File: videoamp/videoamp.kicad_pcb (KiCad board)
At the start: 2 copper layers, 19 x 26 mm, 20 parts, among them J5V1 Conn_01x01, U1 THS7316, U2 AMS1117-3.3

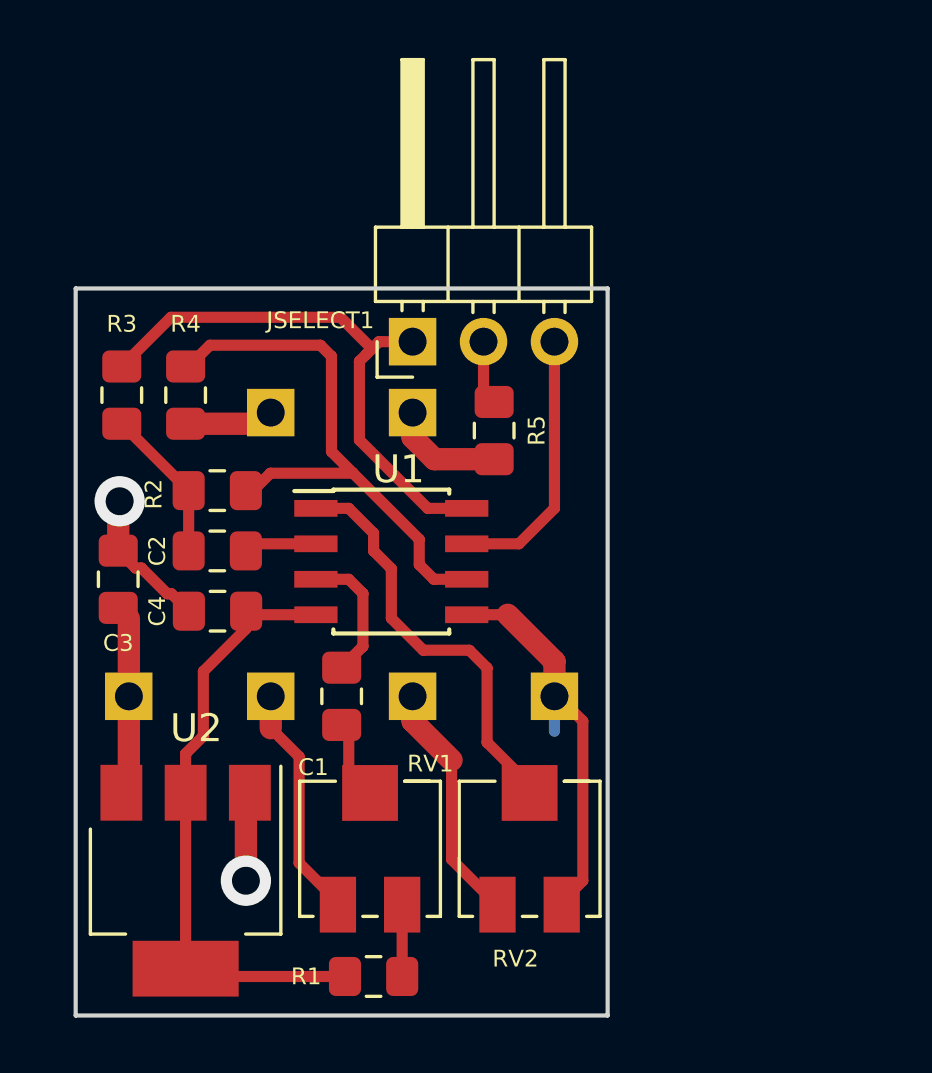
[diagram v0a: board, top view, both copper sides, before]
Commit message: Redesign board to provide luma/chroma/composite signals on A/V out
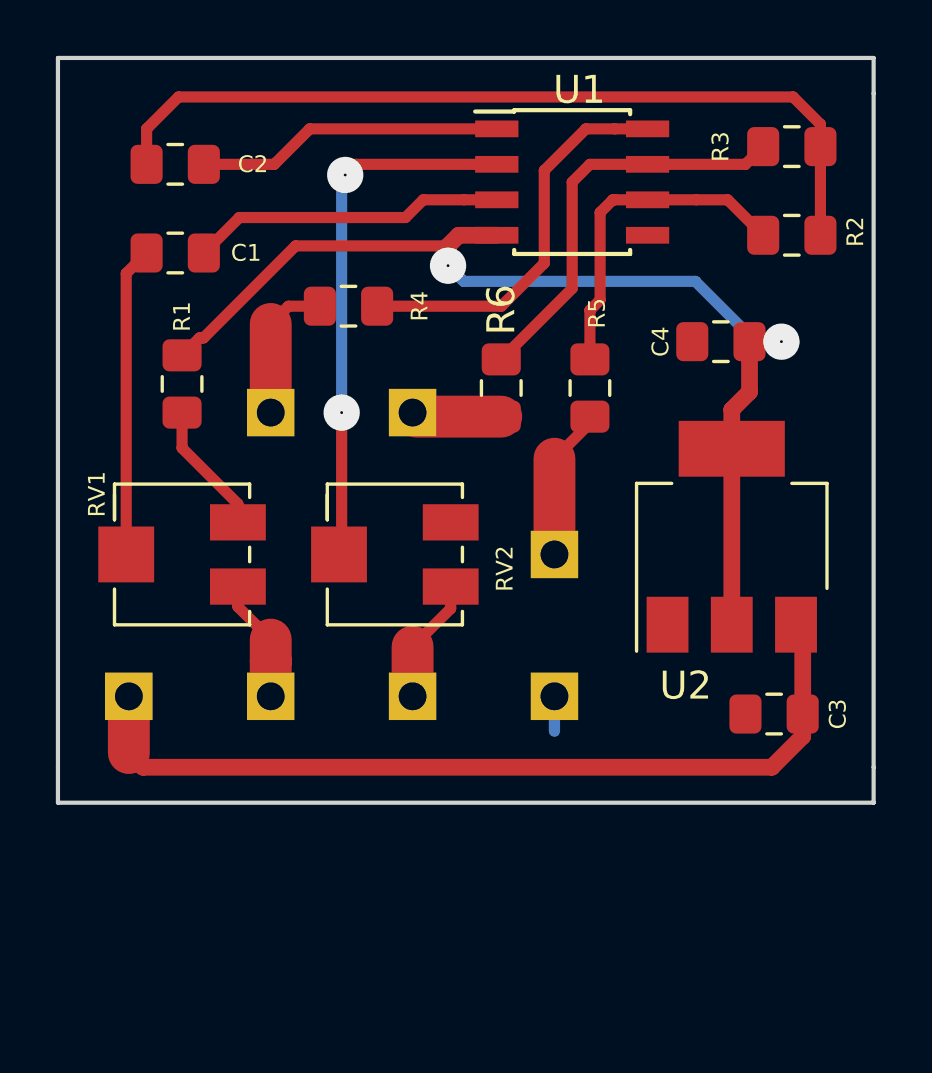
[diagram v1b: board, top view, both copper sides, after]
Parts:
- removed JSELECT1: Conn_01x03, Connector_PinHeader_2.54mm:PinHeader_1x03_P2.54mm_Horizontal
- added JAV6: Conn_01x01, Connector_PinHeader_2.54mm:PinHeader_1x01_P2.54mm_Vertical, B.Cu at (157.5, 116.8)
- added R6: 75, Resistor_SMD:R_0805_2012Metric_Pad1.15x1.40mm_HandSolder, F.Cu at (158.8, 110.9)
- moved R3 25.6 mm to (166.0, 102.2), turned to 180 degrees
- moved C3 24.0 mm to (165.3, 122.6), turned to 180 degrees
- moved U2 23.1 mm to (163.8, 116.2), turned to 90 degrees
- moved R2 22.5 mm to (166.0, 105.4), turned to 180 degrees
- moved R1 22.3 mm to (144.1, 110.7), turned to 270 degrees
- moved C4 20.4 mm to (163.4, 109.2)
- moved C1 17.0 mm to (143.9, 106.0), turned to 0 degrees
- moved U1 15.1 mm to (158.1, 103.5)
- moved C2 13.9 mm to (143.9, 102.9)
- moved RV1 12.5 mm to (144.1, 116.8), turned to 0 degrees
- moved RV2 11.6 mm to (151.8, 116.8), turned to 0 degrees
- moved R4 6.65 mm to (150.1, 108.0), turned to 0 degrees
- moved JAV4 5.08 mm to (147.3, 111.8)
- moved JAV5 5.08 mm to (152.4, 111.8)
- moved R5 1.55 mm to (155.6, 110.9)
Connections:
- R4 pad 1: Net-(JAV5-Pad1) -> Net-(JAV4-Pad1)
- R4 pad 2: /LUMA -> /COMPOSITE
- R5 pad 1: Net-(JAV4-Pad1) -> Net-(JAV5-Pad1)
- R5 pad 2: Net-(JSELECT1-Pad2) -> /CHROMA
- RV1 pad 2: Net-(C1-Pad2) -> Net-(C1-Pad1)
- U1 pad 1: Net-(RV2-Pad2) -> Net-(C2-Pad2)
- U1 pad 2: Net-(C2-Pad2) -> Net-(RV2-Pad2)
- U1 pad 3: Net-(C1-Pad1) -> Net-(C1-Pad2)
- U1 pad 7: /COMPOSITE -> /CHROMA
- U1 pad 8: /CHROMA -> /COMPOSITE
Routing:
- net Net-(C2-Pad1): track 5.66 -> 30.3 mm
- net +5V: track 6.89 -> 30.9 mm
- net GND: track 23.0 -> 1.25 mm, vias 2 -> 0
- net +3V3: track 22.1 -> 38.4 mm, vias 0 -> 2
- net Net-(C2-Pad2): track 2.56 -> 11.0 mm
- net Net-(C1-Pad2): track 2.86 -> 11.3 mm
- net /LUMA: track 20.3 -> 12.0 mm
- net Net-(C1-Pad1): track 4.87 -> 11.1 mm
- net Net-(JAV6-Pad1): track 0.00 -> 5.46 mm
- net /CHROMA: track 20.0 -> 14.8 mm
- net /COMPOSITE: track 9.64 -> 14.3 mm
- net Net-(RV2-Pad2): track 15.0 -> 19.3 mm, vias 0 -> 2
- net Net-(JCHROMA1-Pad1): track 8.74 -> 4.50 mm
- net Net-(JLUMA1-Pad1): track 8.46 -> 4.42 mm
- net Net-(JSELECT1-Pad2): track 2.32 -> 0.00 mm
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- added copper zone on F.Cu, net GND
- removed copper zone on B.Cu, net GND
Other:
- board size 19 x 26 mm -> 29.2 x 26.7 mm
- net class Default: via_dia 1.8 -> 1.3
